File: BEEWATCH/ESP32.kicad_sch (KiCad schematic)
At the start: 35 parts, among them U4 W25Q128JVS

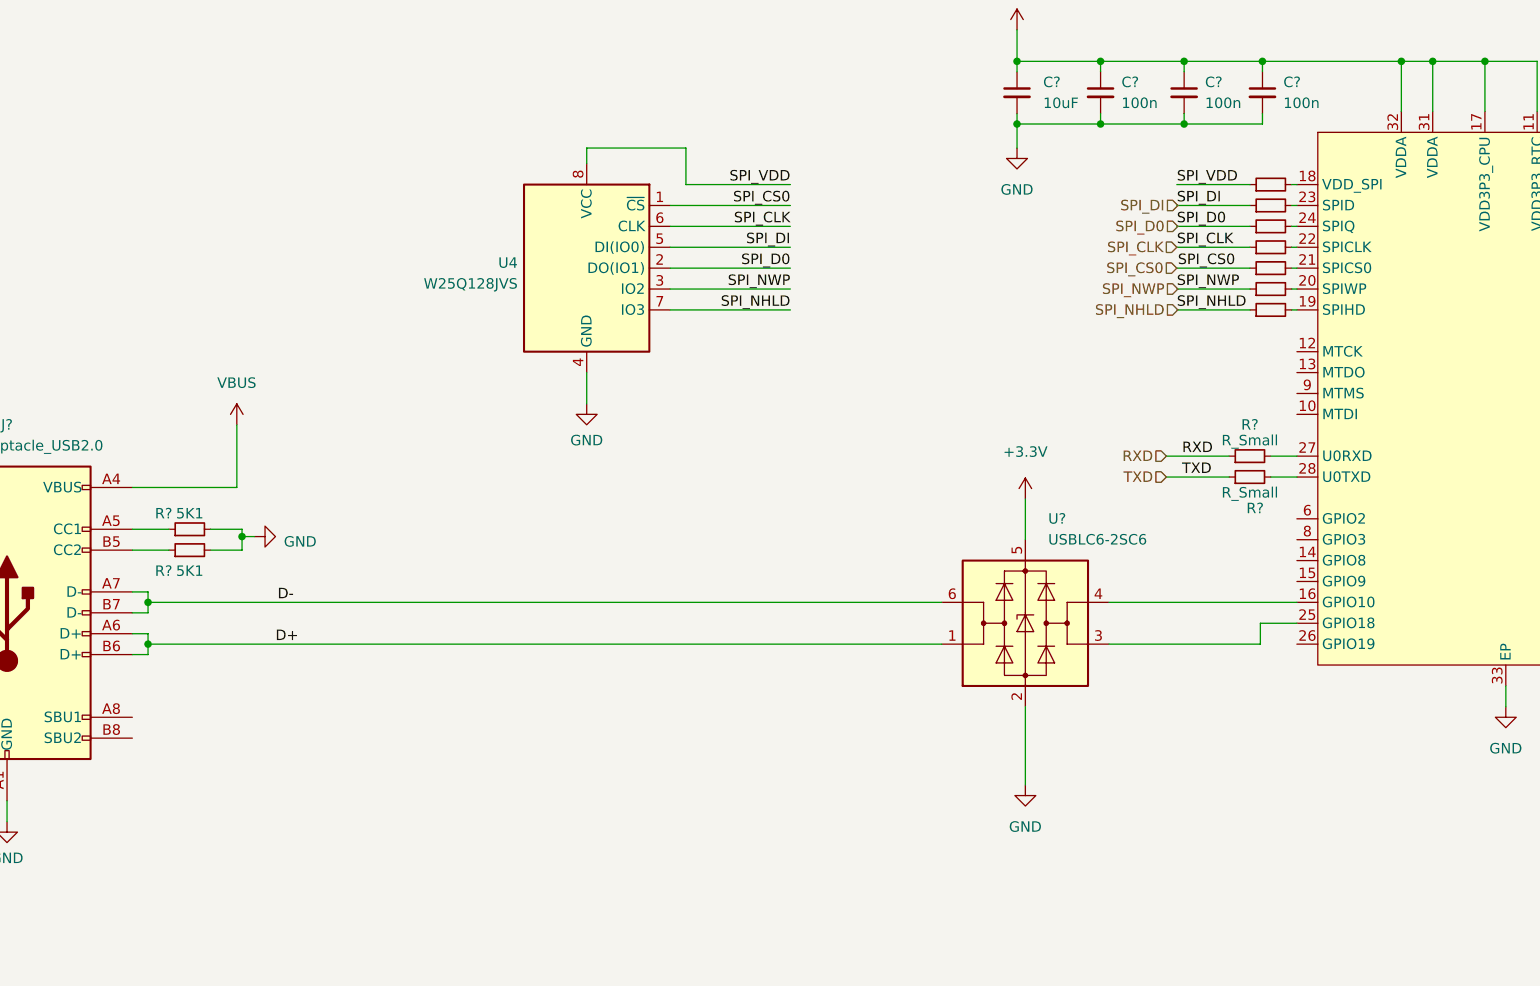
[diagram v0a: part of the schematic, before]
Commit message: GPS Removed
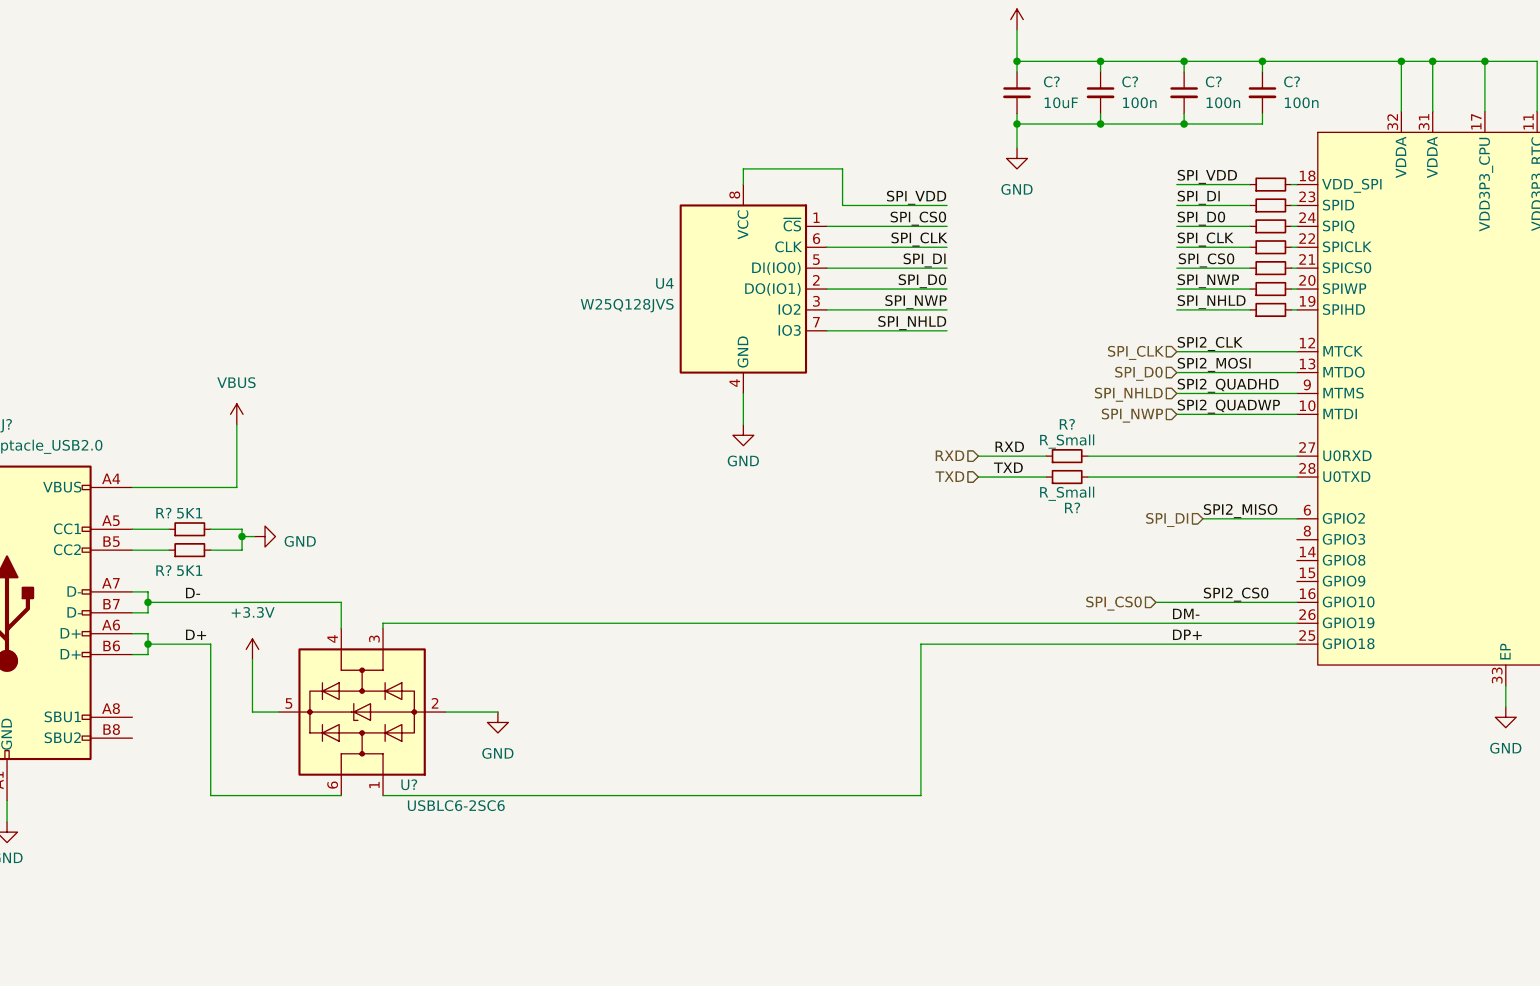
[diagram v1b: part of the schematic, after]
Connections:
- net D+: now also U?.6 (I/O1); no longer U?.1 (I/O1)
- net D-: now also U?.4 (I/O2); no longer U?.6 (I/O1)
- net SPI_CLK: now also U?.12 (MTCK)
- net SPI_CS0: now also U?.16 (GPIO10)
- net SPI_D0: now also U?.13 (MTDO)
- net SPI_DI: now also U?.6 (GPIO2)
- net SPI_NHLD: now also U?.9 (MTMS)
- net SPI_NWP: now also U?.10 (MTDI)
- net DM-: now reaches U?.3 (I/O2)
- net DM-: now also U?.26 (GPIO19); no longer U?.25 (GPIO18)
- new net DP+: U?.1 (I/O1), U?.25 (GPIO18)
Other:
- moved on the sheet: R?, U4, U?
